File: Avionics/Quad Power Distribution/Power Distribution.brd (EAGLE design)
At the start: 49.5 x 49.2 mm, 12 parts

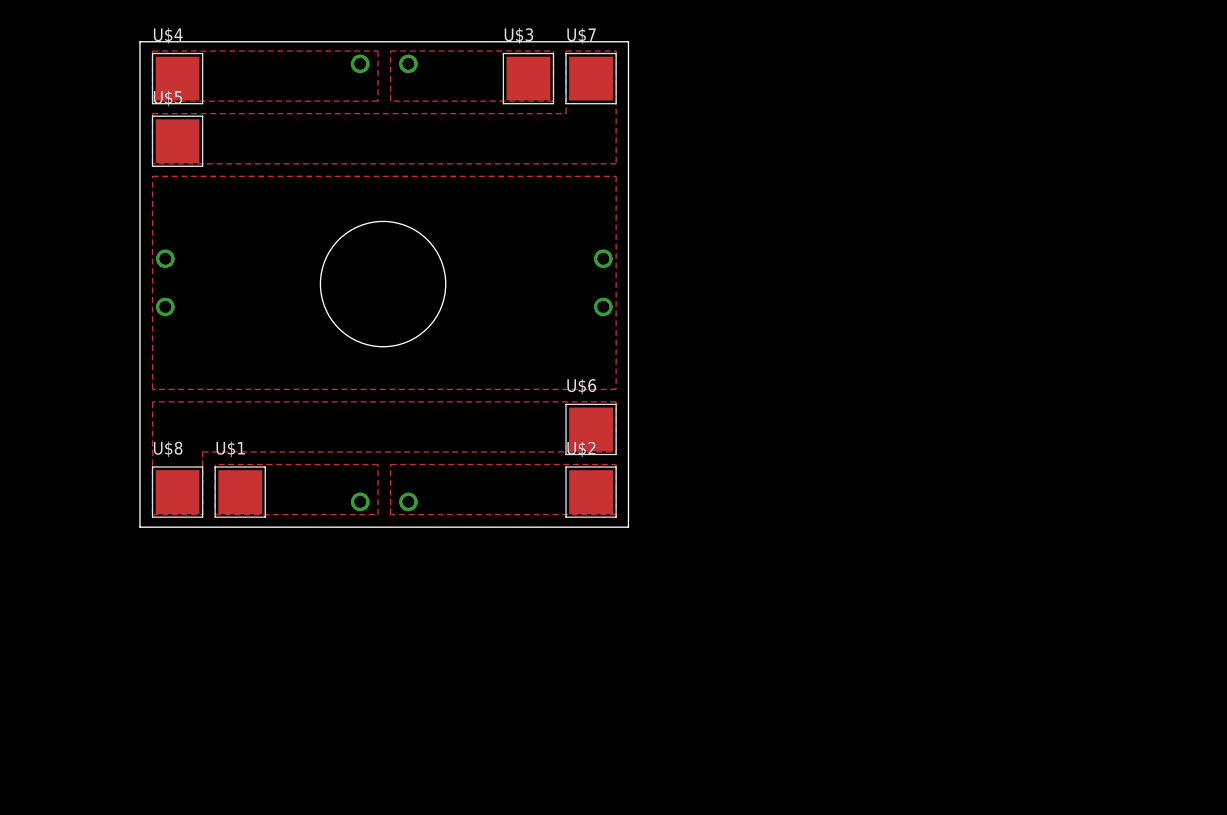
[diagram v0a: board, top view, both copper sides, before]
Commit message: Added current sense circuits and most of the switching regulator.
Need to add signal splitters and output pins.
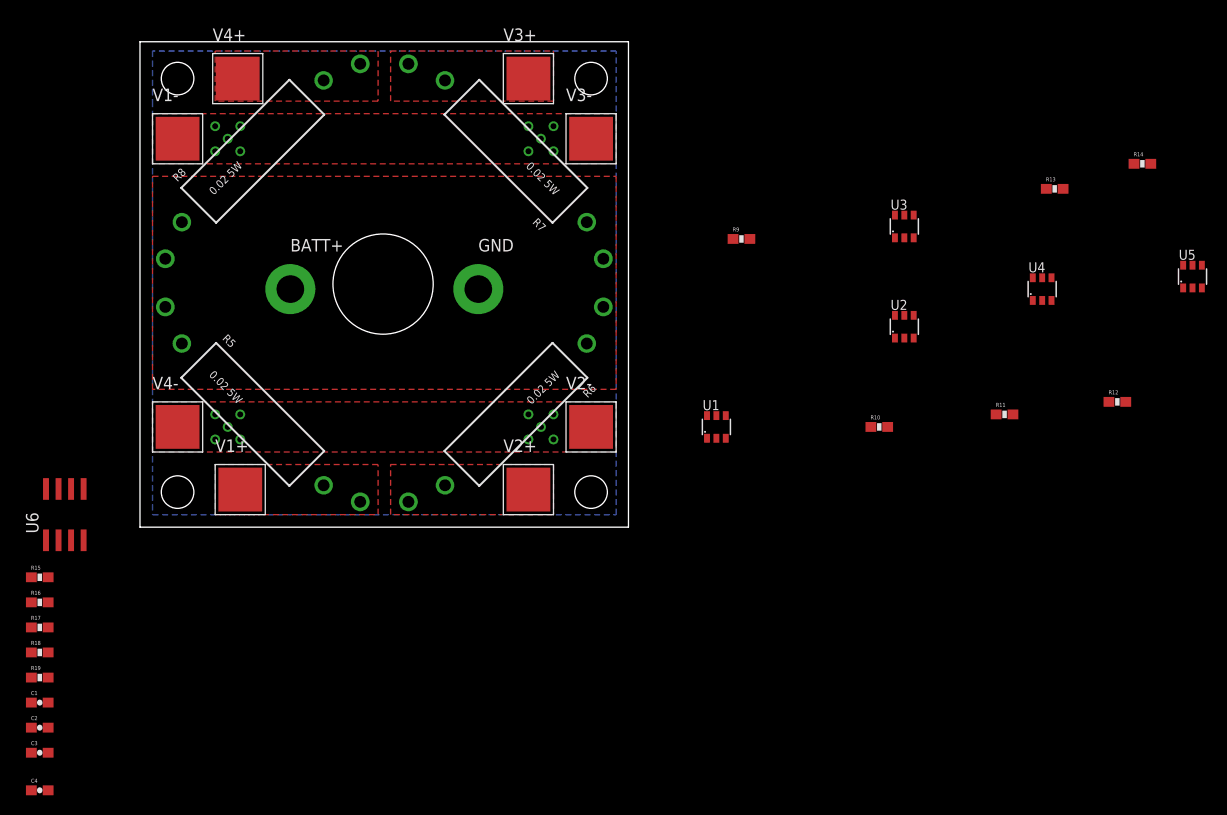
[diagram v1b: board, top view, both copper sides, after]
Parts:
- removed U$5, U$6, U$7, U$8: 3.5MM-BULLET-PLUG5MM-PAD, Shared Libraries:5MMPLUG
- added BATT+, GND: 10AWG_PAD, Shared Libraries:10AWG_SOLDERPAD
- added C1: 10uF, SparkFun-Capacitors:0603-CAP
- added C2, C3: 22uF, SparkFun-Capacitors:0603-CAP
- added C4: 0.1uF, SparkFun-Capacitors:0603-CAP
- added R10, R11, R12, R9: 100K, Shared Libraries:0603-RES
- added R13: 124K, Shared Libraries:0603-RES
- added R14: 0.1, Shared Libraries:0603-RES
- added R15: 100k, Shared Libraries:0603-RES
- added R16: 56k, Shared Libraries:0603-RES
- added R17: 10.2k, Shared Libraries:0603-RES
- added R18: 52.3k, Shared Libraries:0603-RES
- added R19: 10k, Shared Libraries:0603-RES
- added R5, R6, R7, R8: 0.02 5W, Shared Libraries:AXIAL-0.8
- added U1, U2, U3, U4, U5: LMP8645, Shared Libraries:SOT23-6
- added U6: ADP2302, Shared Libraries:SOIC8
- added V1+, V1-, V2+, V2-, V3+, V3-, V4+, V4-: 3.5MM-BULLET-PLUG5MM-PAD, Shared Libraries:5MMPLUG
- R1, R2, R3, R4: value 0.01 5W -> 0.02 5W
- U$1, U$2, U$3, U$4: value 3.5MM-BULLET-PLUG5MM-PAD -> (none); device Shared Libraries:5MMPLUG -> SparkFun-Electromechanical:STAND-OFF
- moved U$3 6.35 mm to (45.7, 45.5)
- moved U$1 6.35 mm to (3.81, 3.56)
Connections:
- new net 5V: R14.1, U1.6, U2.6, U3.6, U4.6, U5.3, U5.6
- new net 5VOUT: R14.2, U5.4
- new net ISENSE1: U1.1
- new net ISENSE2: U2.1
- new net ISENSE3: U3.1
- new net ISENSE4: U4.1
- new net ISENSE5V: U5.1
- new net N$1: R10.2, U2.5
- new net N$10: R18.1, R19.2, U6.5
- new net N$11: R15.1, U6.4
- new net N$12: R16.2, R17.1, U6.3
- new net N$2: R9.2, U1.5
- new net N$3: R11.2, U3.5
- new net N$4: R12.2, U4.5
- new net N$5: R13.2, U5.5
- new net N$6: R15.2, R16.1, U6.2
- new net N$7: C4.1, U6.1
- new net N$8: C4.2, U6.8
- new net N$9: C2.1, C3.1, R18.2
- net GND: now also C2.2, C3.2, GND.P1, R10.1, R11.1, R12.1, R13.1, R19.1, R9.1, U1.2, U2.2, U3.2, U4.2, U5.2, U6.7, V1-.P$1, V2-.P$1, V3-.P$1, V4-.P$1; no longer U$5.P$1, U$6.P$1, U$7.P$1, U$8.P$1
- net V1+: now also R5.P$2, U1.4, V1+.P$1; no longer U$1.P$1
- net V2+: now also R6.P$2, U2.4, V2+.P$1; no longer U$2.P$1
- net V3+: now also R7.P$2, U3.4, V3+.P$1; no longer U$3.P$1
- net V4+: now also R8.P$2, U4.4, V4+.P$1; no longer U$4.P$1
- net VBATT+: now also BATT+.P1, R5.P$1, R6.P$1, R7.P$1, R8.P$1, U1.3, U2.3, U3.3, U4.3
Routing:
- added copper zone on layer 16, net GND

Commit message: Finished switcher circuit, almost there.
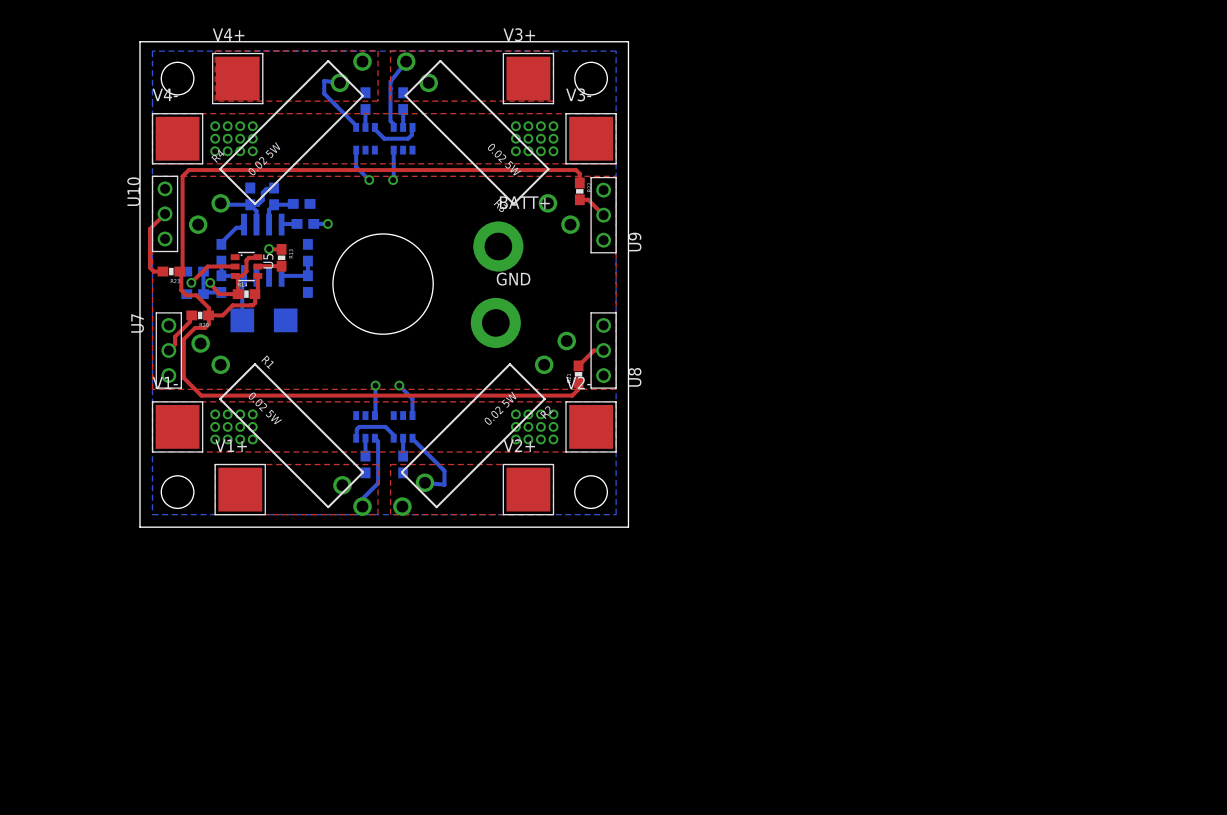
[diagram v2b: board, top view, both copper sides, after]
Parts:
- added D1: SSB43L, diode:SMB
- added L1: 10uH, SparkFun-Passives:0603
- added R20, R21, R22, R23: 0, Shared Libraries:0603-RES
- added U10, U7, U8, U9: SERVOPLUGTHROUGHHOLE_0.1PITCH, Shared Libraries:0.1-PITCH-3CONN
- R1, R2, R3, R4: device Shared Libraries:AXIAL-1.1 -> Shared Libraries:AXIAL-0.8
- moved U5 95.9 mm to (10.8, 26.4), turned to 270 degrees
- moved R14 91.8 mm to (10.8, 23.6)
- moved R12 82.1 mm to (22.9, 43.2), flipped to the bottom, turned to 270 degrees
- moved R13 78.7 mm to (14.4, 27.3), turned to 270 degrees
- moved U4 70.3 mm to (22.9, 39.4), flipped to the bottom
- moved R11 68.7 mm to (26.7, 43.2), flipped to the bottom, turned to 270 degrees
- moved C4 57.5 mm to (8.26, 27.8), flipped to the bottom, turned to 270 degrees
- moved C1 55.6 mm to (11.2, 33.5), flipped to the bottom, turned to 90 degrees
- moved U2 51.8 mm to (26.7, 10.2), flipped to the bottom, turned to 180 degrees
- moved U3 51.6 mm to (26.7, 39.4), flipped to the bottom
- moved C3 51.2 mm to (5.59, 25.9), flipped to the bottom
- moved R19 50.9 mm to (17.0, 27.8), flipped to the bottom, turned to 270 degrees
- moved R17 50.5 mm to (16.4, 32.8), flipped to the bottom, turned to 180 degrees
- moved R10 48.4 mm to (26.7, 6.35), flipped to the bottom, turned to 90 degrees
- moved R16 47.5 mm to (13.6, 33.5), flipped to the bottom, turned to 270 degrees
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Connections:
- removed net N$6: R15.2, R16.1, U6.2
- new net N$13: R21.2, U8.2
- new net N$14: R22.2, U9.2
- new net N$15: R23.2, U10.2
- new net S1: U7.3
- new net S2: U8.3
- new net S3: U9.3
- new net S4: U10.3
- net 5V: now also C2.1, C3.1, L1.2, R18.2
- net 5VOUT: now also R20.1, R21.1, R22.1, R23.1
- net GND: now also C1.2, D1.A, R17.2, U10.1, U7.1, U8.1, U9.1
- net N$8: now also D1.C, L1.1
- net N$9: now also R20.2, U7.2; no longer C2.1, C3.1, R18.2
- net VBATT+: now also C1.1, R15.2, R16.1, U6.2
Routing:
- net 5VOUT: track 0.00 -> 115.4 mm
- net 5V: track 0.00 -> 25.1 mm, vias 0 -> 1
- net VBATT+: track 0.00 -> 23.7 mm, vias 0 -> 5
- net N$8: track 0.00 -> 8.46 mm
- net V2+: track 0.00 -> 8.04 mm
- net V1+: track 0.00 -> 7.85 mm
- net V4+: track 0.00 -> 7.66 mm
- net N$15: track 0.00 -> 7.56 mm
- net V3+: track 0.00 -> 7.34 mm
- net GND: track 0.00 -> 6.41 mm, vias 20 -> 50
- net N$9: track 0.00 -> 4.52 mm
- net N$12: track 0.00 -> 4.20 mm
- net N$10: track 0.00 -> 4.16 mm
- net N$13: track 0.00 -> 3.35 mm
- net N$7: track 0.00 -> 3.21 mm
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
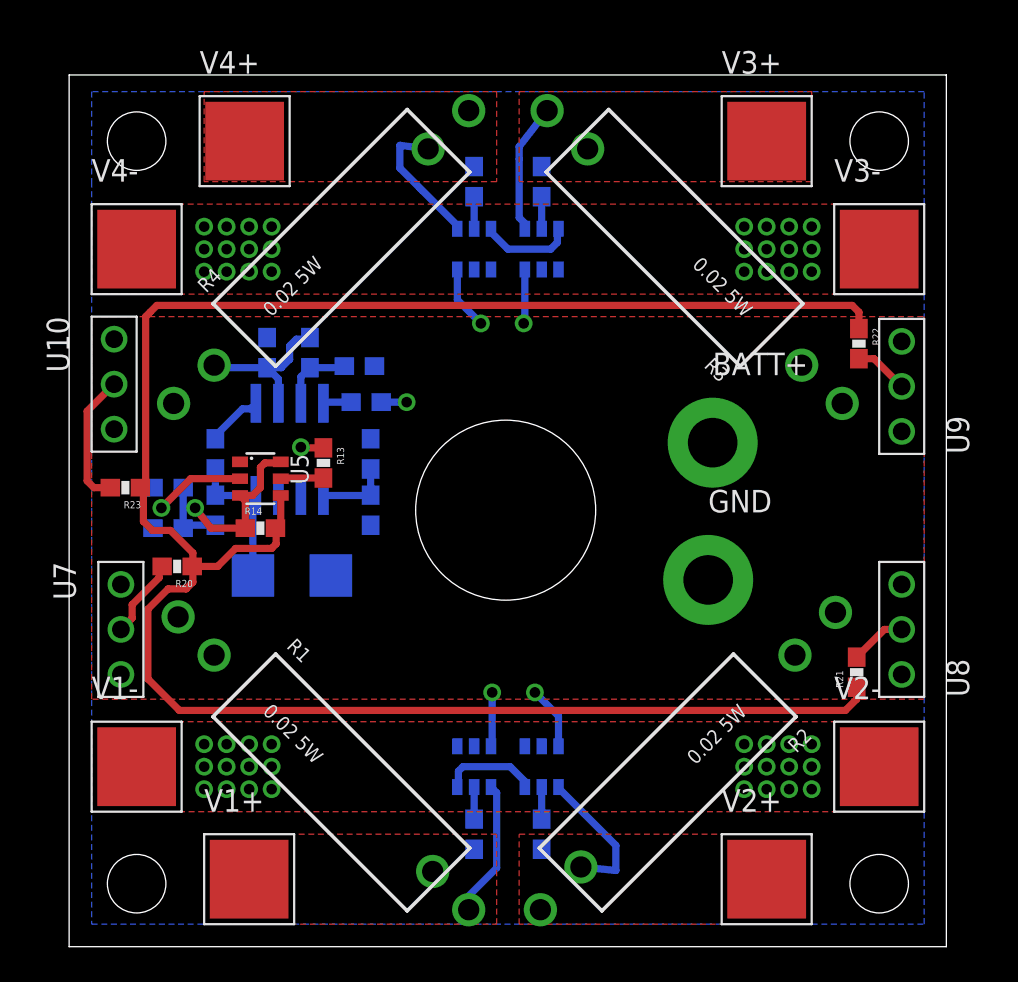
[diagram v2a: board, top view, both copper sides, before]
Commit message: Completed layout and routing. Adding vias later
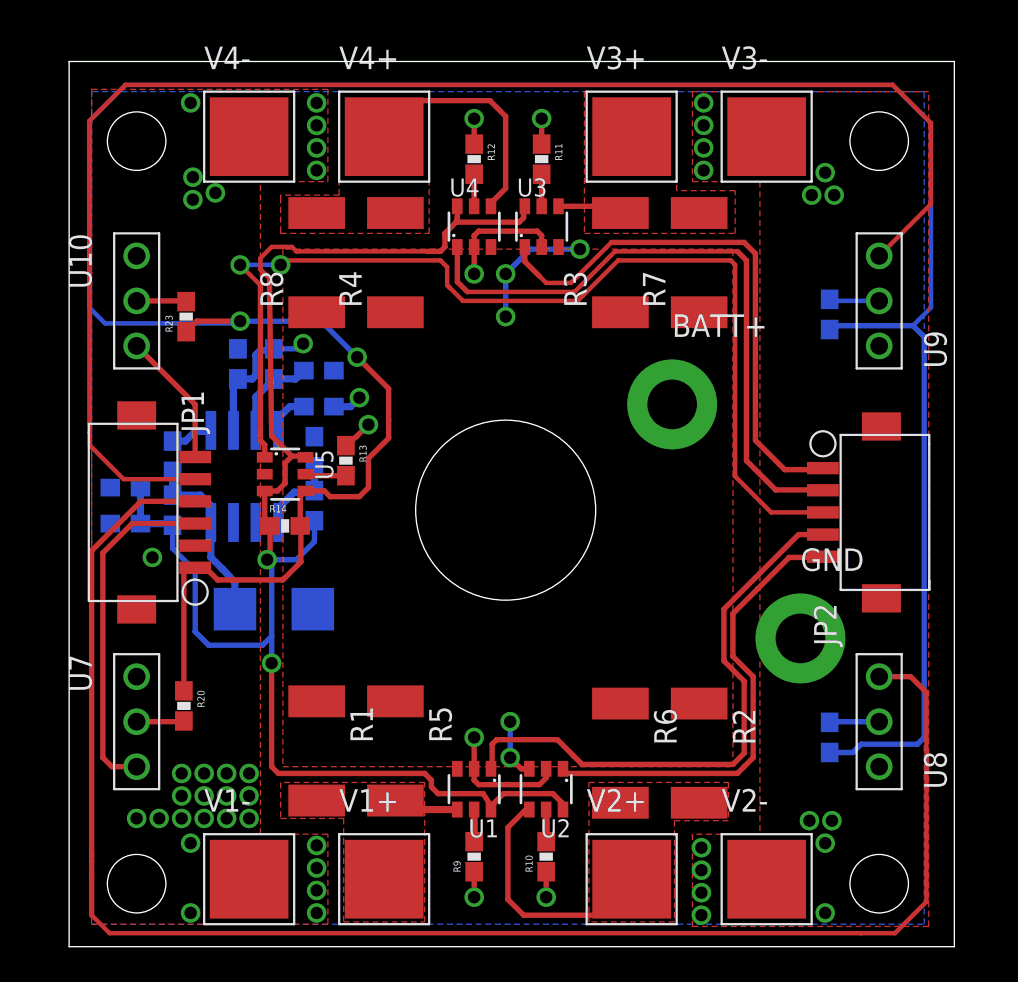
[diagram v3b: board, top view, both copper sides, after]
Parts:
- added JP1: (no value), Shared Libraries:DF13_6POS
- added JP2: (no value), Shared Libraries:DF13_5POS
- R1, R2, R3, R4, R5, R6, R7, R8: device Shared Libraries:AXIAL-0.8 -> Shared Libraries:R2512
- moved R23 10.2 mm to (6.60, 35.6), turned to 90 degrees
- moved V2- 8.98 mm to (39.4, 3.81)
- moved V3- 8.98 mm to (39.4, 45.7)
- moved V4- 8.98 mm to (10.2, 45.7)
- moved V1- 8.98 mm to (10.2, 3.81)
- moved R20 7.88 mm to (6.48, 13.6), turned to 270 degrees
- moved V4+ 7.88 mm to (17.8, 45.7)
- moved V3+ 7.62 mm to (31.8, 45.7)
- moved V1+ 7.62 mm to (17.8, 3.81)
- moved V2+ 7.62 mm to (31.8, 3.81)
- moved GND 6.17 mm to (41.3, 17.4)
- moved U8 5.36 mm to (45.7, 12.7)
- moved U7 5.28 mm to (3.81, 12.7)
- moved R5 5.09 mm to (18.4, 11.0), flipped to the top, turned to 270 degrees
- moved R6 5.01 mm to (31.1, 10.9), flipped to the top, turned to 270 degrees
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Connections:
- net 5VOUT: now also JP1.P1
- net GND: now also JP1.P2
- net ISENSE1: now also JP2.P4
- net ISENSE2: now also JP2.P5
- net ISENSE3: now also JP2.P1
- net ISENSE4: now also JP2.P2
- net ISENSE5V: now also JP2.P3
- net S1: now also JP1.P3
- net S2: now also JP1.P4
- net S3: now also JP1.P5
- net S4: now also JP1.P6
- net V1+: now also R1.2, R5.2; no longer R1.P$2, R5.P$2
- net V2+: now also R2.2, R6.2; no longer R2.P$2, R6.P$2
- net V3+: now also R3.2, R7.2; no longer R3.P$2, R7.P$2
- net V4+: now also R4.2, R8.2; no longer R4.P$2, R8.P$2
- net VBATT+: now also R1.1, R2.1, R3.1, R4.1, R5.1, R6.1, R7.1, R8.1; no longer R1.P$1, R2.P$1, R3.P$1, R4.P$1, R5.P$1, R6.P$1, R7.P$1, R8.P$1
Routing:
- net S2: track 0.00 -> 90.7 mm
- net S3: track 0.00 -> 83.0 mm
- net 5V: track 25.1 -> 88.3 mm, vias 1 -> 2
- net ISENSE5V: track 0.00 -> 59.8 mm, vias 0 -> 2
- net 5VOUT: track 115.4 -> 160.8 mm, vias 0 -> 2
- net ISENSE4: track 0.00 -> 36.0 mm
- net ISENSE1: track 0.00 -> 32.5 mm
- net ISENSE3: track 0.00 -> 30.6 mm
- net ISENSE2: track 0.00 -> 26.3 mm
- net S1: track 0.00 -> 19.6 mm
- net GND: track 6.41 -> 21.6 mm, vias 50 -> 51
- net S4: track 0.00 -> 7.64 mm
- net V3+: track 7.34 -> 2.10 mm
- net N$15: track 7.56 -> 2.81 mm
- net V1+: track 7.85 -> 3.81 mm
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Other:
- board size 49.5 x 49.2 mm -> 50 x 50 mm

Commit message: Cleaned up silk
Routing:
- net GND: vias 51 -> 85

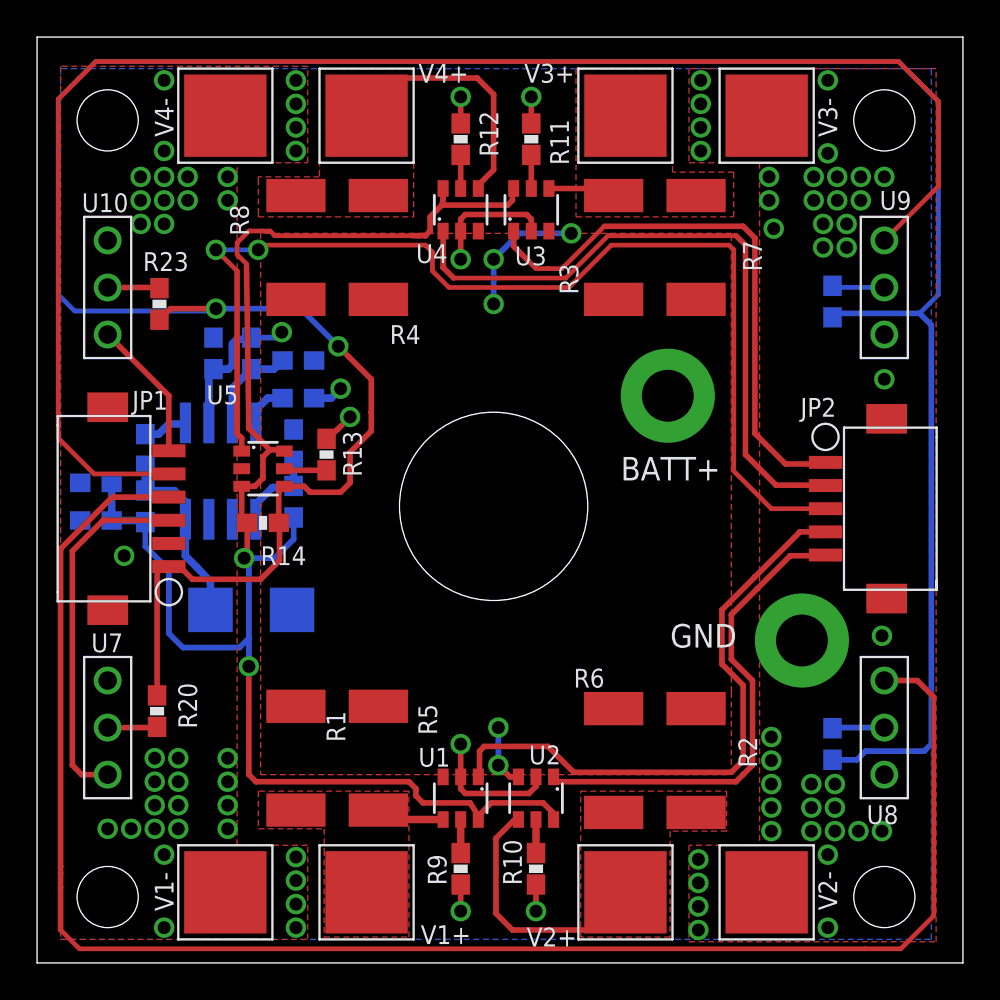
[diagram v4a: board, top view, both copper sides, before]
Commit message: Added more silk and changed vias to tented small circles
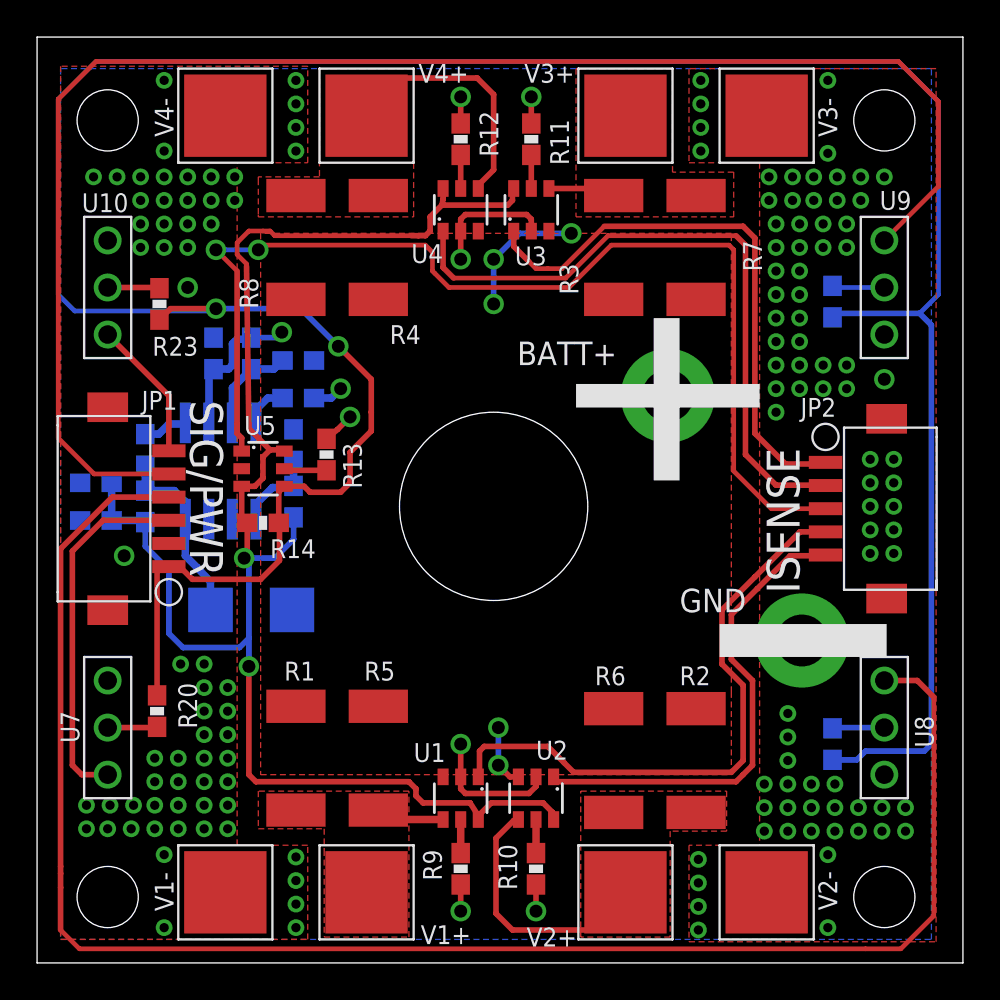
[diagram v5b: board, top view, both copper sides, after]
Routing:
- net GND: vias 85 -> 150
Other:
- board text added: "ISENSE"
- board text added: "MOTOR 1"
- board text added: "MOTOR 2"
- board text added: "MOTOR 3"
- board text added: "MOTOR 4"
- board text added: "SIG/PWR"
